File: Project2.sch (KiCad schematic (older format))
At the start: 75 parts, among them J1 Header_8-Y1Y8, J10 CON-USB-MICROAB, J2 Header_8-X9X16, J3 Header_X17X24, J4 Header_8-P1P8, J5 MicroSD-PUSH_PULL, J6 Proj2Battery, J7 Header_P9P10, J8 Header_8-Y9Y16, J9 Header_8-X1X8, Q1 DMP2160UW, SW1 RST, SW2 USR, U1 STM32F405RGT6, U2 MCP1702, U3 MMA7660FC, U4 MIC2005A-1YM5-TR, Y1 32.768 kHz, Y2 12 MHz

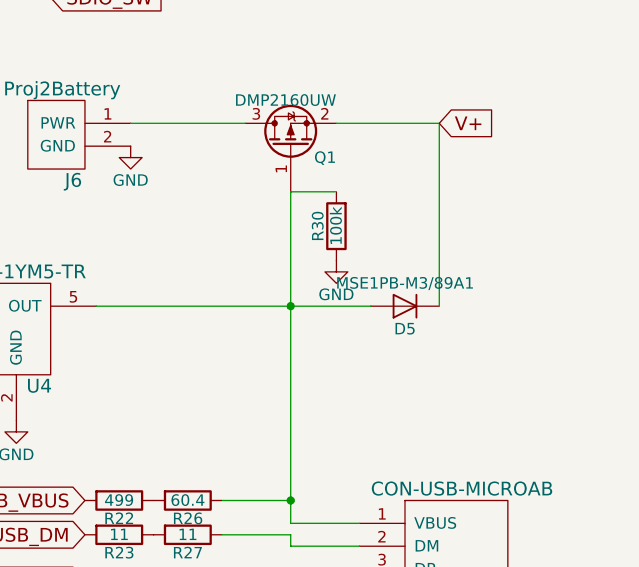
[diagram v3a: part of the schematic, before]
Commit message: Consolidated footprints to one library
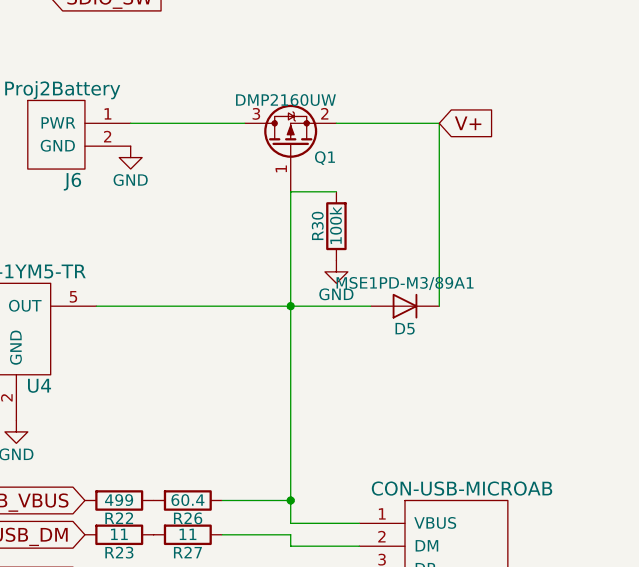
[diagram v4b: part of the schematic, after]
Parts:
- D5: value MSE1PB-M3/89A1 -> MSE1PD-M3/89A1
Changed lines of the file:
@@
 P 13800 3750
 F 0 "D5" H 13800 3850 50  0000 C CNN
-F 1 "MSE1PB-M3/89A1" H 13800 3650 50  0000 C CNN
+F 1 "MSE1PD-M3/89A1" H 13800 3650 50  0000 C CNN
 F 2 "" H 13800 3750 50  0001 C CNN
 F 3 "" H 13800 3750 50  0001 C CNN

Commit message: Finished schematic, created a couple footprints, started layout
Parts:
- added R99: 4.75k, Resistors_SMD:R_0603, symbol R
- D5: footprint (none) -> Project2Footprints:Diode
- J1, J2, J3, J4, J8, J9: footprint (none) -> Project2Footprints:1x8_Header
- J10: footprint (none) -> Project2Footprints:USB_microB_2040002-1
- J5: footprint (none) -> Project2Footprints:MicroSD
- J6: footprint (none) -> Project2Footprints:Battery
- J7: footprint (none) -> Project2Footprints:2x4_Header
- Q1: footprint (none) -> Project2Footprints:MOSFET
- SW1, SW2: footprint (none) -> Project2Footprints:Switch
- U1: footprint (none) -> Project2Footprints:MicrocontrollerFootprint
- U2: footprint (none) -> Project2Footprints:VoltageRegulator
- U3: footprint (none) -> Project2Footprints:Accelerometer
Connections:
- net 3V3: now also R99.1
- net GND: now also U2.1 (GND)
- net SCL_X9: now also U3.6 (SCL)
- net SDA_X10: now also U3.7 (SDA)
- net SW_X17: now also R99.2
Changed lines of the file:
@@
 F 0 "U1" H 3150 1750 60  0000 C CNN
 F 1 "STM32F405RGT6" H 3150 5150 60  0000 C CNN
-F 2 "" H 3750 4150 60  0001 C CNN
+F 2 "Project2Footprints:MicrocontrollerFootprint" H 3750 4150 60  0001 C CNN
 F 3 "" H 3750 4150 60  0001 C CNN
 	1    3000 3050
@@
 F 0 "U1" H 3300 5400 60  0000 C CNN
 F 1 "STM32F405RGT6" H 3300 7300 60  0000 C CNN
-F 2 "" H 3900 7350 60  0001 C CNN
+F 2 "Project2Footprints:MicrocontrollerFootprint" H 3900 7350 60  0001 C CNN
 F 3 "" H 3900 7350 60  0001 C CNN
 	2    3150 6250
@@
 F 0 "U1" H 3600 9550 60  0000 C CNN
 F 1 "STM32F405RGT6" H 3600 10200 60  0000 C CNN
-F 2 "" H 4400 10300 60  0001 C CNN
+F 2 "Project2Footprints:MicrocontrollerFootprint" H 4400 10300 60  0001 C CNN
 F 3 "" H 4400 10300 60  0001 C CNN
 	3    3650 9200
@@
 F 0 "U1" H 3950 10850 60  0000 C CNN
 F 1 "STM32F405RGT6" H 4050 11800 60  0000 C CNN
-F 2 "" H 4800 11850 60  0001 C CNN
+F 2 "Project2Footprints:MicrocontrollerFootprint" H 4800 11850 60  0001 C CNN
 F 3 "" H 4800 11850 60  0001 C CNN
 	4    4050 10750
@@
 Text GLabel 4100 2850 2    60   Input ~ 0
 Y12
-Text GLabel 4100 3050 2    60   Input ~ 0
+Text GLabel 4700 3050 2    60   Input ~ 0
 SW_X17
 Text GLabel 4100 3150 2    60   Input ~ 0
@@
 F 0 "J4" H 12400 8000 60  0000 C CNN
 F 1 "Header_8-P1P8" H 11900 8000 60  0000 C CNN
-F 2 "" H 12100 8300 60  0001 C CNN
+F 2 "Project2Footprints:1x8_Header" H 12100 8300 60  0001 C CNN
 F 3 "" H 12100 8300 60  0001 C CNN
 	1    12100 8300
@@
 F 0 "J9" H 14100 7850 60  0000 C CNN
 F 1 "Header_8-X1X8" H 14000 8800 60  0000 C CNN
-F 2 "" H 14000 8250 60  0001 C CNN
+F 2 "Project2Footprints:1x8_Header" H 14000 8250 60  0001 C CNN
 F 3 "" H 14000 8250 60  0001 C CNN
 	1    14000 8250
@@
 F 0 "J2" H 11000 7200 60  0000 C CNN
 F 1 "Header_8-X9X16" H 10850 8100 60  0000 C CNN
-F 2 "" H 10950 7850 60  0001 C CNN
+F 2 "Project2Footprints:1x8_Header" H 10950 7850 60  0001 C CNN
 F 3 "" H 10950 7850 60  0001 C CNN
 	1    10950 7850
@@
 F 0 "J1" H 10950 6300 60  0000 C CNN
 F 1 "Header_8-Y1Y8" H 10800 7200 60  0000 C CNN
-F 2 "" H 10950 6850 60  0001 C CNN
+F 2 "Project2Footprints:1x8_Header" H 10950 6850 60  0001 C CNN
 F 3 "" H 10950 6850 60  0001 C CNN
 	1    10950 6850
@@
 F 0 "J8" H 14050 6800 60  0000 C CNN
 F 1 "Header_8-Y9Y16" H 14050 7750 60  0000 C CNN
-F 2 "" H 14000 7200 60  0001 C CNN
+F 2 "Project2Footprints:1x8_Header" H 14000 7200 60  0001 C CNN
 F 3 "" H 14000 7200 60  0001 C CNN
 	1    14000 7200
@@
 F 0 "J7" H 13450 8100 60  0000 C CNN
 F 1 "Header_P9P10" H 13200 8600 60  0000 C CNN
-F 2 "" H 13200 8350 60  0001 C CNN
+F 2 "Project2Footprints:2x4_Header" H 13200 8350 60  0001 C CNN
 F 3 "" H 13200 8350 60  0001 C CNN
 	1    13200 8350
@@
 F 0 "J3" H 12450 8750 60  0000 C CNN
 F 1 "Header_X17X24" H 12050 9050 60  0000 C CNN
-F 2 "" H 12050 8950 60  0001 C CNN
+F 2 "Project2Footprints:1x8_Header" H 12050 8950 60  0001 C CNN
 F 3 "" H 12050 8950 60  0001 C CNN
 	1    12050 8950
@@
 F 0 "U3" H 7900 6500 60  0000 C CNN
 F 1 "MMA7660FC" H 7550 7200 60  0000 C CNN
-F 2 "" H 7450 6800 60  0001 C CNN
+F 2 "Project2Footprints:Accelerometer" H 7450 6800 60  0001 C CNN
 F 3 "" H 7450 6800 60  0001 C CNN
 	1    7450 6800
@@
 F 0 "J10" H 14250 4650 60  0000 C CNN
 F 1 "CON-USB-MICROAB" H 14050 5350 60  0000 C CNN
-F 2 "" H 14050 4950 60  0001 C CNN
+F 2 "Project2Footprints:USB_microB_2040002-1" H 14050 4950 60  0001 C CNN
 F 3 "" H 14050 4950 60  0001 C CNN
 	1    14050 4950
@@
 F 0 "D5" H 13800 3850 50  0000 C CNN
 F 1 "MSE1PD-M3/89A1" H 13800 3650 50  0000 C CNN
-F 2 "" H 13800 3750 50  0001 C CNN
+F 2 "Project2Footprints:Diode" H 13800 3750 50  0001 C CNN
 F 3 "" H 13800 3750 50  0001 C CNN
 	1    13800 3750
@@
 F 0 "Q1" V 13250 2850 50  0000 L CNN
 F 1 "DMP2160UW" V 13500 2850 50  0000 L CNN
-F 2 "" H 13500 3150 50  0001 C CNN
+F 2 "Project2Footprints:MOSFET" H 13500 3150 50  0001 C CNN
 F 3 "" H 13300 3050 50  0001 C CNN
 	1    13300 3050
@@
 F 0 "J6" H 12350 2700 60  0000 C CNN
 F 1 "Proj2Battery" H 12300 3100 60  0000 C CNN
-F 2 "" H 12350 2950 60  0001 C CNN
+F 2 "Project2Footprints:Battery" H 12350 2950 60  0001 C CNN
 F 3 "" H 12350 2950 60  0001 C CNN
 	1    12350 2950
@@
 F 0 "U2" H 5900 9850 60  0000 C CNN
 F 1 "MCP1702" H 5650 10350 60  0000 C CNN
-F 2 "" H 5600 10050 60  0001 C CNN
+F 2 "Project2Footprints:VoltageRegulator" H 5600 10050 60  0001 C CNN
 F 3 "" H 5600 10050 60  0001 C CNN
 	1    5600 10050
@@
 Wire Wire Line
 	5200 10400 6100 10400
-Connection ~ 5750 10400
 Wire Wire Line
 	5200 10400 5200 10200
-Connection ~ 5550 10400
 $Comp
 L GND #PWR022
@@
 F 0 "J5" H 12750 750 60  0000 C CNN
 F 1 "MicroSD-PUSH_PULL" H 12300 1650 60  0000 C CNN
-F 2 "" H 12250 1300 60  0001 C CNN
+F 2 "Project2Footprints:MicroSD" H 12250 1300 60  0001 C CNN
 F 3 "" H 12250 1300 60  0001 C CNN
 	1    12250 1300
@@
 $EndComp
 Wire Wire Line
-	1300 9200 1300 9000
+	1300 9000 1300 9200
 $Comp
 L C C1
@@
 F 0 "SW2" H 7600 10225 50  0000 C CNN
 F 1 "USR" H 7600 10000 50  0000 C CNN
-F 2 "" H 7600 10100 50  0001 C CNN
+F 2 "Project2Footprints:Switch" H 7600 10100 50  0001 C CNN
 F 3 "" H 7600 10100 50  0001 C CNN
 	1    7600 10100
@@
 F 0 "SW1" H 1300 8925 50  0000 C CNN
 F 1 "RST" H 1300 8700 50  0000 C CNN
-F 2 "" H 1300 8800 50  0001 C CNN
+F 2 "Project2Footprints:Switch" H 1300 8800 50  0001 C CNN
 F 3 "" H 1300 8800 50  0001 C CNN
 	1    1300 8800
 	0    -1   -1   0
 $EndComp
+Text GLabel 8100 6850 2    60   Input ~ 0
+SDA_X10
+Text GLabel 8100 6950 2    60   Input ~ 0
+SCL_X9
+Wire Wire Line
+	5650 10400 5650 10400
+Connection ~ 5650 10400
+Wire Wire Line
+	4100 3050 4700 3050
+Wire Wire Line
+	4700 3050 4700 2850
+$Comp
+L R R99
+U 1 1 59D597D8
+P 4700 2700
+F 0 "R99" V 4780 2700 50  0000 C CNN
+F 1 "4.75k" V 4700 2700 50  0000 C CNN
+F 2 "Resistors_SMD:R_0603" V 4630 2700 50  0001 C CNN
+F 3 "" H 4700 2700 50  0001 C CNN
+	1    4700 2700
+	1    0    0    -1
+$EndComp
+Text GLabel 4700 2550 1    60   Input ~ 0
+3V3
 $EndSCHEMATC

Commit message: ALL THE SIGNAL PINS
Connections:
- net BOOT0_P1 is gone; now on net BOOT0-P1: J4.1 (P1)
- net USB_DM renamed USB_D_N
- net USB_DP renamed USB_D_P
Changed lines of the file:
@@
 USB_ID
 Text GLabel 4100 2150 2    60   Input ~ 0
-USB_DM
+USB_D_N
 Text GLabel 4100 2250 2    60   Input ~ 0
-USB_DP
+USB_D_P
 Text GLabel 4100 1050 2    60   Input ~ 0
 X1
@@
 SW_X17
 Text GLabel 11650 8150 1    60   Input ~ 0
-BOOT0_P1
+BOOT0-P1
 Text GLabel 11750 8150 1    60   Input ~ 0
 BLU_P2
@@
 USB_VBUS
 Text GLabel 12400 4750 0    60   Input ~ 0
-USB_DM
+USB_D_N
 Text GLabel 12400 4950 0    60   Input ~ 0
-USB_DP
+USB_D_P
 Text GLabel 12400 5150 0    60   Input ~ 0
 USB_ID

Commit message: Finished
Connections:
- net GND: now also J4.7 (P7); no longer J4.8 (P8)
- net V+: now also J4.8 (P8); no longer J4.7 (P7)
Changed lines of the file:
@@
 	4350 8300 4350 8650
 Wire Wire Line
-	4350 8650 5050 8650
-Wire Wire Line
-	5050 8650 5050 8150
+	5050 8650 4350 8650
+Wire Wire Line
+	5050 8150 5050 8650
 $Comp
 L GND #PWR05
@@
 Text GLabel 12650 9450 1    60   Input ~ 0
 A3V3
-Text GLabel 12250 8000 1    60   Input ~ 0
+Text GLabel 12550 8100 1    60   Input ~ 0
 V+
 Wire Wire Line
-	12250 8150 12250 8000
+	12250 7950 12250 8150
 Wire Wire Line
 	12350 8150 12550 8150
 Wire Wire Line
-	12550 8150 12550 8200
+	12550 8150 12550 8100
 $Comp
 L GND #PWR010
 U 1 1 59CBEB10
-P 12550 8200
-F 0 "#PWR010" H 12550 7950 50  0001 C CNN
-F 1 "GND" H 12550 8050 50  0000 C CNN
-F 2 "" H 12550 8200 50  0001 C CNN
-F 3 "" H 12550 8200 50  0001 C CNN
-	1    12550 8200
+P 12350 7950
+F 0 "#PWR010" H 12350 7700 50  0001 C CNN
+F 1 "GND" H 12350 7800 50  0000 C CNN
+F 2 "" H 12350 7950 50  0001 C CNN
+F 3 "" H 12350 7950 50  0001 C CNN
+	1    12350 7950
 	1    0    0    -1
 $EndComp
@@
 Text GLabel 4700 2550 1    60   Input ~ 0
 3V3
+Wire Wire Line
+	12250 7950 12350 7950
 $EndSCHEMATC
